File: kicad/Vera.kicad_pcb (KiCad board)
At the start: 3 copper layers, 69.8 x 25.4 mm, 37 parts, among them Q1 AO3400, T1 Wurth 749010012A, T2 Wurth 749010012A, U1 TI AM62A7, U2 Microchip KSZ9477, U3 TI MSPM0G3507, U4 TI ISOW1044BDFMR, U5 Infineon SLB9670, Y1 25MHz

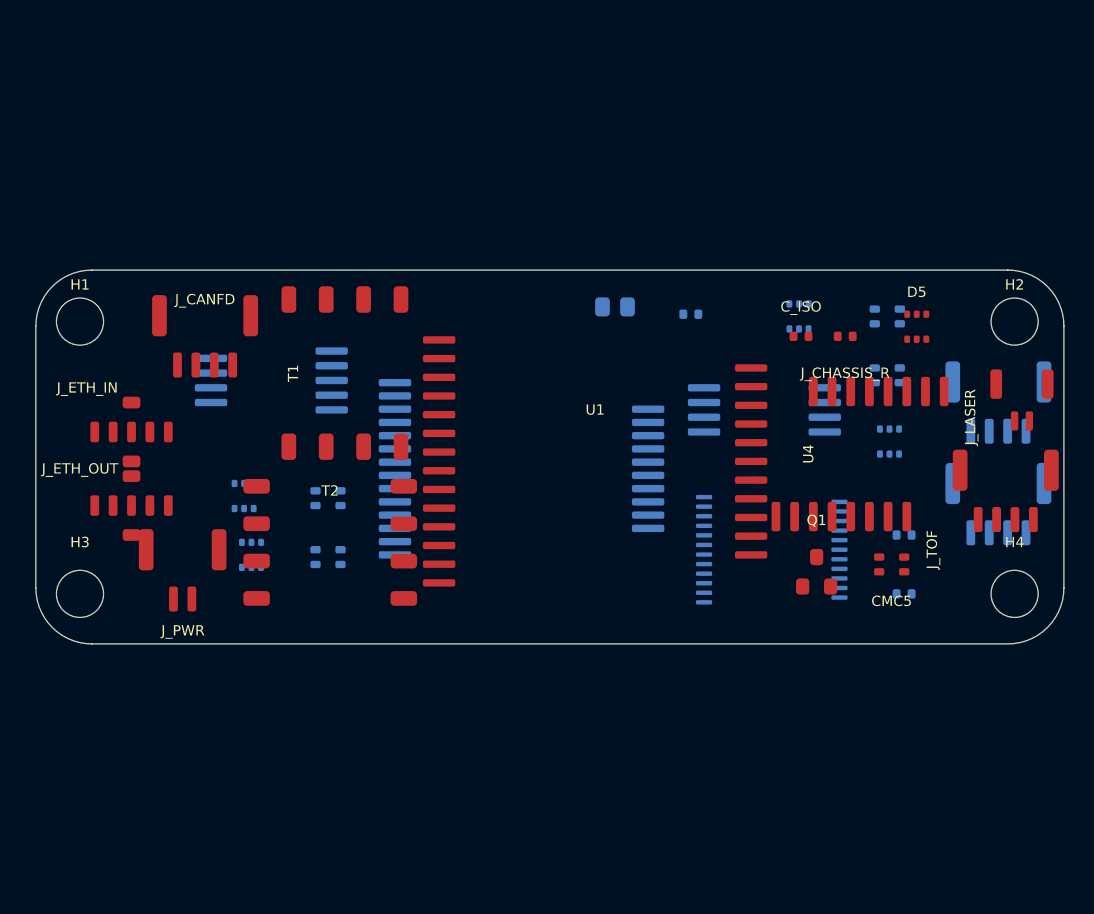
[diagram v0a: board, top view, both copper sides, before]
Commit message: Vera: fix unloadable PCB (restore In2.Cu, rebuild outline) + dot-grid/3D analysis
PCB was committed in a broken state after the 1"-wide (25.4 x 69.85 mm) resize:
- LAYER TABLE was missing In2.Cu(6), leaving an invalid 3-copper-layer stackup ->
  "Failed to load board" (broken across several commits). Restored In2.Cu to the
  4-layer stackup (F.Cu/In1.Cu/In2.Cu/B.Cu), matching Emma. Board loads again.
- Edge.Cuts was malformed/self-intersecting from the resize (invalid_outline x4).
  Rebuilt a clean rounded rectangle 69.85 x 25.4 mm, 3.81 mm corners -> 0 invalid.
- Verified: sch<->pcb net parity is EXACT (88 = 88 nets) -- the nets were never
  scrambled; the board just would not load. Remaining DRC (29 lib_footprint_mismatch,
  silk text) is the pre-existing placeholder-footprint / not-fab-ready state; 106
  unconnected is the never-routed state (routing awaits real footprints).
- Vera.md: corrected the stale mounting-hole coords from the old 46x48 board
  (4,4)/(42,44) -- (42,44) is outside a 25.4 mm-tall board -- to the 69.85x25.4
  pattern (4,4)/(65.85,4)/(4,21.4)/(65.85,21.4).

VERA_LASER_ANALYSIS.md -> Rev B: pattern switched from crosshair to a DOT GRID
(homography for full pose: tilt magnitude+azimuth, no sign ambiguity; cheaper
commodity DOE; better SNR, still Class 2). New cargo TRUE 3D imager (separate
camera+projector by ~75 mm baseline -> ~1.9 mm depth res at 5 ft, pseudo-random
dots); nose stays boresighted grid (baseline useless at 50 ft). Manufacturer notes
(LaserLand / HOLO/OR / Osela / Edmund).

Co-Authored-By: Claude Opus 4.8 <noreply@anthropic.com>
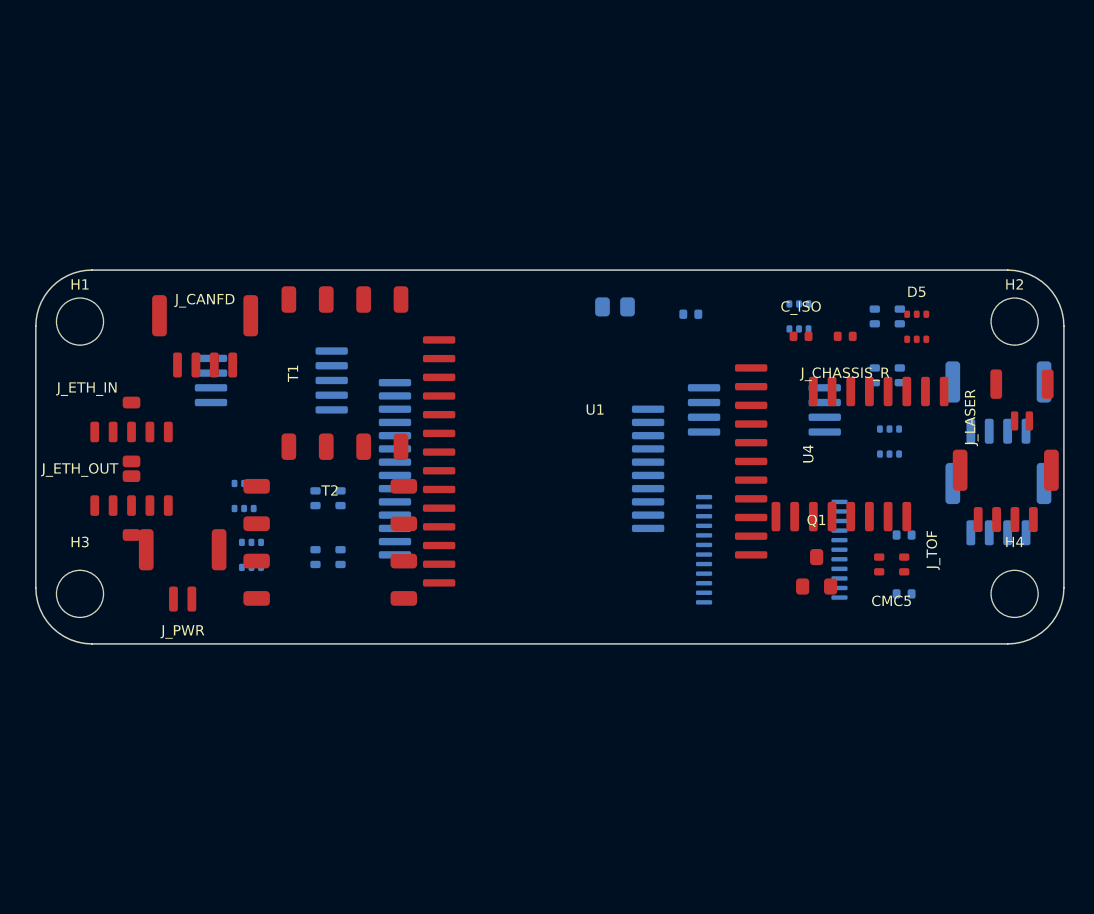
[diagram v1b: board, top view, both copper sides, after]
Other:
- copper layers 3 -> 4
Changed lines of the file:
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@@
 		(0 "F.Cu" signal)
 		(4 "In1.Cu" power)
+		(6 "In2.Cu" power)
 		(2 "B.Cu" power)
 		(9 "F.Adhes" user "F.Adhesive")
@@
 		(embedded_fonts no)
 	)
-	(gr_arc
-		(start 3.81 25.4)
-		(mid 1.115923 24.284077)
-		(end 0 21.59)
-		(stroke
-			(width 0.05)
-			(type solid)
-		)
-		(layer "Edge.Cuts")
-	)
 	(gr_line
 		(start 3.81 0)
-		(end 66.04 0)
+		(end 66.039999 0)
 		(stroke
-			(width 0.05)
-			(type solid)
+			(width 0.1)
+			(type default)
 		)
 		(layer "Edge.Cuts")
 	)
 	(gr_line
-		(start 69.85 3.81)
-		(end 69.85 21.59)
+		(start 66.039999 25.4)
+		(end 3.81 25.4)
 		(stroke
-			(width 0.05)
-			(type solid)
+			(width 0.1)
+			(type default)
 		)
 		(layer "Edge.Cuts")
 	)
-	(gr_line
-		(start 65.989353 25.399663)
-		(end 3.81 25.4)
+	(gr_arc
+		(start 66.039999 0)
+		(mid 68.734076 1.115923)
+		(end 69.85 3.81)
 		(stroke
-			(width 0.05)
-			(type solid)
+			(width 0.1)
+			(type default)
 		)
 		(layer "Edge.Cuts")
 	)
-	(gr_line
-		(start 0 21.59)
-		(end 0 3.81)
+	(gr_arc
+		(start 69.85 21.59)
+		(mid 68.734076 24.284076)
+		(end 66.039999 25.4)
 		(stroke
-			(width 0.05)
-			(type solid)
+			(width 0.1)
+			(type default)
 		)
 		(layer "Edge.Cuts")
@@
 		(end 3.81 0)
 		(stroke
-			(width 0.05)
-			(type solid)
+			(width 0.1)
+			(type default)
 		)
 		(layer "Edge.Cuts")
 	)
-	(gr_arc
-		(start 66.04 0)
-		(mid 68.734077 1.115923)
-		(end 69.85 3.81)
+	(gr_line
+		(start 69.85 3.81)
+		(end 69.85 21.59)
 		(stroke
-			(width 0.05)
-			(type solid)
+			(width 0.1)
+			(type default)
+		)
+		(layer "Edge.Cuts")
+	)
+	(gr_line
+		(start 0 21.59)
+		(end 0 3.81)
+		(stroke
+			(width 0.1)
+			(type default)
 		)
 		(layer "Edge.Cuts")
 	)
 	(gr_arc
-		(start 69.85 21.59)
-		(mid 68.734077 24.284077)
-		(end 66.04 25.4)
+		(start 3.81 25.4)
+		(mid 1.115923 24.284076)
+		(end 0 21.59)
 		(stroke
-			(width 0.05)
-			(type solid)
+			(width 0.1)
+			(type default)
 		)
 		(layer "Edge.Cuts")

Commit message: Vera: place direct-solder sensor lands on the PCB (pcbnew transform)
mod_vera_ds_pcb.py adds J_TOF_DS/J_LASER_DS/J_CAM_DS (from Vera.pretty) to the
hand-maintained Vera.kicad_pcb in place (NOT regenerated -- the board is GUI-owned
and carries the In2.Cu/outline hand-fixes). Each pad is netted to its JST
counterpart's exact net (verified: CSI_CLK_*/CSI_D0_*/CAM_*/+3V3/GND on the camera
land; +5V/GND/UART_TOF_* on ToF; +5V/LASER_CATHODE on laser).

Verified after transform: board loads in kicad-cli; copper stackup intact
(F.Cu/In1.Cu/In2.Cu/B.Cu -- In2.Cu preserved, no recurrence of the drop bug);
invalid_outline = 0.

Lands seeded in a row at the aperture-relative X spacing (ToF..laser 8.2mm,
ToF..camera 16.5mm per bow_sensor_pod.scad). FINAL XY/rotation + which edge faces
the pod is a MANUAL mechanical fit to the sensor mounting plate -- any placement
overlap/clearance DRC on this tightly-packed board is referred to the user per the
project footprint-placement rule.

Co-Authored-By: Claude Opus 4.8 <noreply@anthropic.com>
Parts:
- added J_CAM_DS: DS_Camera_9P, DS_Camera_9P, F.Cu at (21.0, 6.00)
- added J_LASER_DS: DS_Laser_2P, DS_Laser_2P, F.Cu at (12.7, 6.00)
- added J_TOF_DS: DS_ToF_4P, DS_ToF_4P, F.Cu at (4.50, 6.00)

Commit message: Vera: align direct-solder lands to board frame (port-starboard Y spread)
Per the Vera board frame (user): +X fore->aft, +Y starboard->port, +Z
ventral->dorsal; sensors forward, network aft. The three nose apertures differ in
the PORT-STARBOARD (Y) axis, so the lands are respread along Y (not X as first
seeded), co-located with their sensor JST counterparts:
  J_TOF_DS   Y=5.0   (starboard, low Y)
  J_LASER_DS Y=13.2  (centreline, +8.2mm)   <- aperture spacing, bow_sensor_pod.scad
  J_CAM_DS   Y=21.5  (port, +16.5mm)
all at X=62 (just inboard of the sensor JST cluster at X~65-67).
mod_vera_ds_pcb.py now repositions idempotently. Board loads; In2.Cu + outline
intact; nets unchanged.

FLAG -- fore/aft mismatch to resolve: the current board places the SENSOR
connectors at HIGH X (~65-67) and the NETWORK connectors at LOW X (~6-11). Per the
stated convention (sensors forward = low X, network aft = high X) this is
FORE-AFT-FLIPPED. The DS lands are co-located with the sensors as-built (high X);
if the board should match the convention, the whole sensor/network cluster
assignment needs to swap ends -- referred to user.

Co-Authored-By: Claude Opus 4.8 <noreply@anthropic.com>
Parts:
- moved J_TOF_DS 57.5 mm to (62.0, 5.00)
- moved J_LASER_DS 49.8 mm to (62.0, 13.2)
- moved J_CAM_DS 43.8 mm to (62.0, 21.5)
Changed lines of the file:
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@@
 	(footprint "DS_Camera_9P"
 		(layer "F.Cu")
-		(at 21 6)
+		(at 62 21.5)
 		(property "Reference" "J_CAM_DS"
 			(at 0 -2.2 0)
@@
 	(footprint "DS_Laser_2P"
 		(layer "F.Cu")
-		(at 12.7 6)
+		(at 62 13.2)
 		(property "Reference" "J_LASER_DS"
 			(at 0 -2.2 0)
@@
 	(footprint "DS_ToF_4P"
 		(layer "F.Cu")
-		(at 4.5 6)
+		(at 62 5)
 		(property "Reference" "J_TOF_DS"
 			(at 0 -2.2 0)

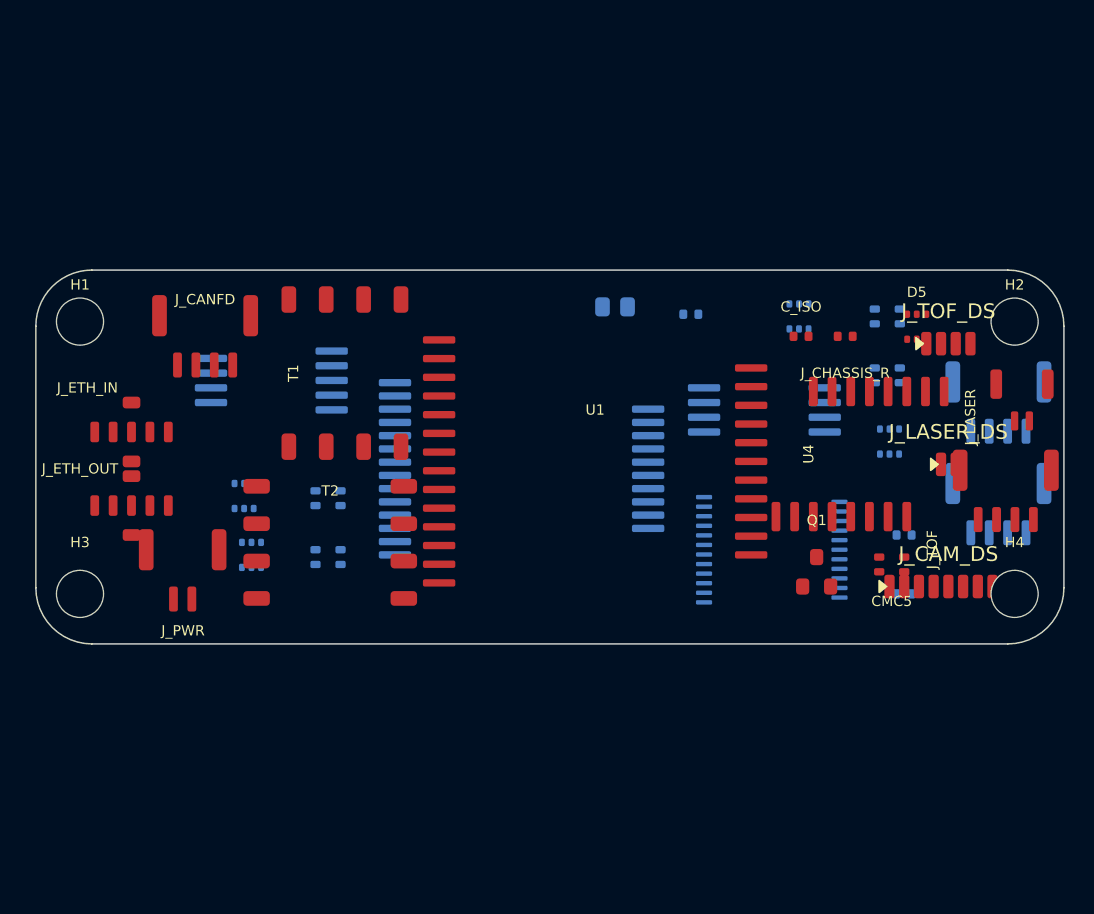
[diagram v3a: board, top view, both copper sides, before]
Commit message: Vera: redraw PCB outline as the nose trapezoid (candidate)
mod_vera_trapezoid.py redraws Edge.Cuts as the trapezoid from
docs/VERA_NOSE_TRAPEZOID.md Rev B: narrow 25.4mm at the fwd/sensor end (high X),
widening to 58mm at the aft end (low X), 69.85mm long, symmetric about the board
centreline (~aircraft CL). Fits the measured ~58mm usable nose interior and holds
the 40x40 SoM at the aft end.

Verified: board loads (pre-commit guard), invalid_outline=0, copper stackup intact
(In2.Cu preserved). Outline extents X -0.1..69.9, Y -16.4..41.8. This is a CANDIDATE
straight trapezoid; a fast-widening/two-segment nose-following edge is the FreeCAD
refinement (doc 4.1/6). Existing placeholder footprints not yet re-placed -> the
edge-clearance DRC delta is expected and resolves when components are laid out for
the trapezoid (gated on the SoM 270-pad DSC + ISOW1044 DFM-20 footprints).

Co-Authored-By: Claude Opus 4.8 <noreply@anthropic.com>
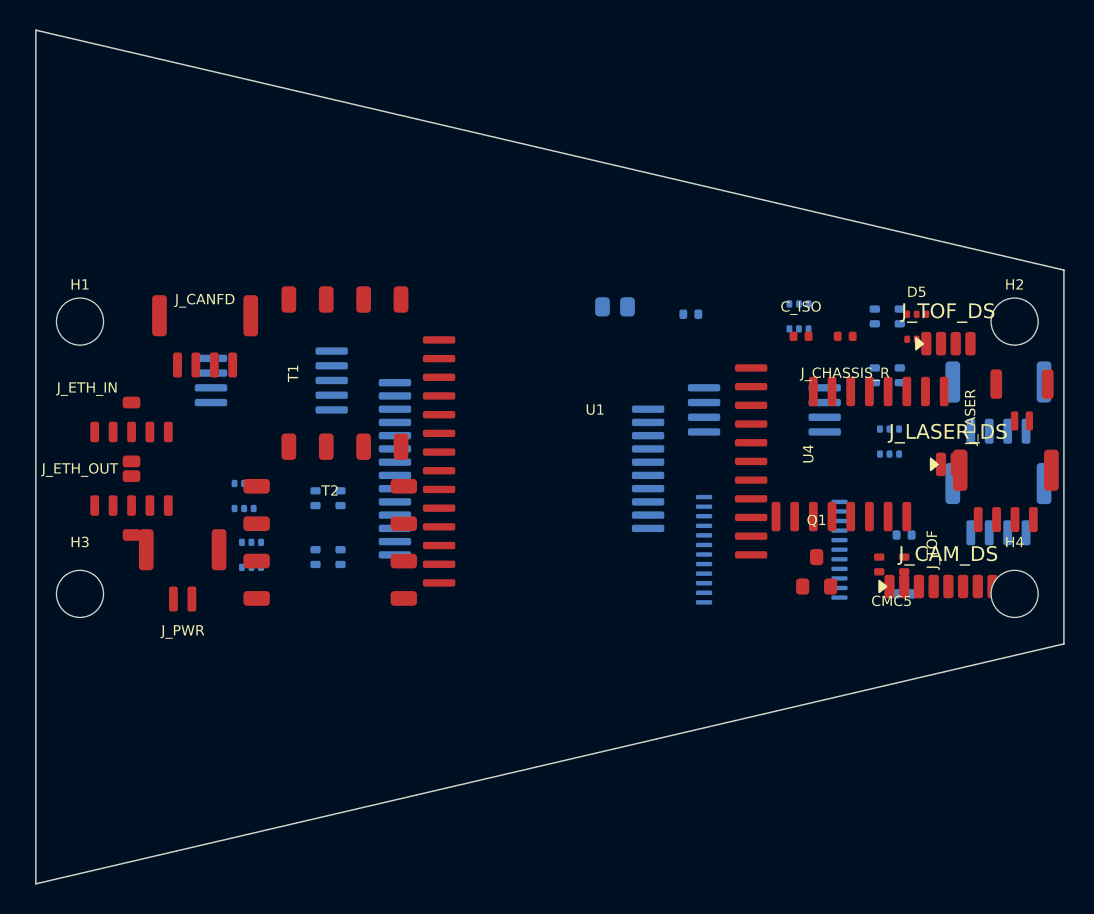
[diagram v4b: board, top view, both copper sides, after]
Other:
- board size 69.8 x 25.4 mm -> 69.8 x 58 mm
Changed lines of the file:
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@@
 	)
 	(gr_line
-		(start 3.81 0)
-		(end 66.039999 0)
+		(start 0 -16.3)
+		(end 69.85 0)
 		(stroke
 			(width 0.1)
@@
 	)
 	(gr_line
-		(start 66.039999 25.4)
-		(end 3.81 25.4)
-		(stroke
-			(width 0.1)
-			(type default)
-		)
-		(layer "Edge.Cuts")
-	)
-	(gr_arc
-		(start 66.039999 0)
-		(mid 68.734076 1.115923)
-		(end 69.85 3.81)
-		(stroke
-			(width 0.1)
-			(type default)
-		)
-		(layer "Edge.Cuts")
-	)
-	(gr_arc
-		(start 69.85 21.59)
-		(mid 68.734076 24.284076)
-		(end 66.039999 25.4)
-		(stroke
-			(width 0.1)
-			(type default)
-		)
-		(layer "Edge.Cuts")
-	)
-	(gr_arc
-		(start 0 3.81)
-		(mid 1.115923 1.115923)
-		(end 3.81 0)
+		(start 0 41.7)
+		(end 0 -16.3)
 		(stroke
 			(width 0.1)
@@
 	)
 	(gr_line
-		(start 69.85 3.81)
-		(end 69.85 21.59)
+		(start 69.85 25.4)
+		(end 0 41.7)
 		(stroke
 			(width 0.1)
@@
 	)
 	(gr_line
-		(start 0 21.59)
-		(end 0 3.81)
+		(start 69.85 0)
+		(end 69.85 25.4)
 		(stroke
 			(width 0.1)
-			(type default)
-		)
-		(layer "Edge.Cuts")
-	)
-	(gr_arc
-		(start 3.81 25.4)
-		(mid 1.115923 24.284076)
-		(end 0 21.59)
-		(stroke
-			(width 0.1)

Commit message: Vera: place PCM-071 SoM at aft/wide end -- initial two-sided fit confirmed
mod_vera_som_place.py adds U_SOM (phyCORE-AM62x PCM-071 placement footprint, 32x43)
at the aft/wide end (board X=24, Y=12.7, rot90 so 43mm runs fore-aft). Verified the
32mm-wide module fits the nose trapezoid: 36.8mm board width at the SoM forward edge
vs 32mm needed; ~57mm at the aft. Board loads (pre-commit guard), invalid_outline=0,
stackup intact.

Initial 2-sided fit: SoM + sensor DS lands/JSTs (fwd) + network conns (aft) all fit
the trapezoid. Old raw-SoC placeholders (U1 AM62A7, U_PMIC) not yet removed -> their
overlap DRC is expected and clears in the full connector-variant re-layout (drop
raw-SoC parts, add the Samtec BTH-060 land pattern + carrier ICs, wire per net map).

Co-Authored-By: Claude Opus 4.8 <noreply@anthropic.com>
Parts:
- added U_SOM: phyCORE-AM62x_PCM071, phyCORE-AM62x_PCM071_placement, F.Cu at (24.0, 12.7)
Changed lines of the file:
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@@
+		(embedded_fonts no)
+	)
+	(footprint "phyCORE-AM62x_PCM071_placement"
+		(layer "F.Cu")
+		(at 24 12.7 90)
+		(descr "PHYTEC phyCORE-AM62x PCM-071 connectorized SoM -- PLACEMENT footprint (outline + 2x M2.5 mounting holes + 2 Samtec BTH-060 connector reference zones) from PHYTEC HW manual L-1038e.A5 Figs 3/6/7. For fit/placement only; the 240 BTH-060 solder pads (A1..D60, 0.5mm pitch 2x60 x2) require the Samtec BTH-060-01-L-D-A-K-TR land pattern -- author before routing. 32x43mm, 5mm connector stacking height.")
+		(property "Reference" "U_SOM"
+			(at 0 -23 90)
+			(layer "F.SilkS")
+			(effects
+				(font
+					(size 1 1)
+					(thickness 0.15)
+				)
+			)
+		)
+		(property "Value" "phyCORE-AM62x_PCM071"
+			(at 0 23 90)
+			(layer "F.Fab")
+			(effects
+				(font
+					(size 1 1)
+					(thickness 0.15)
+				)
+			)
+		)
+		(property "Datasheet" ""
+			(at 0 0 90)
+			(layer "F.Fab")
+			(hide yes)
+			(effects
+				(font
+					(size 1.27 1.27)
+					(thickness 0.15)
+				)
+			)
+		)
+		(property "Description" ""
+			(at 0 0 90)
+			(layer "F.Fab")
+			(hide yes)
+			(effects
+				(font
+					(size 1.27 1.27)
+					(thickness 0.15)
+				)
+			)
+		)
+		(attr exclude_from_pos_files exclude_from_bom allow_missing_courtyard)
+		(fp_rect
+			(start -16 -21.5)
+			(end 16 21.5)
+			(stroke
+				(width 0.12)
+				(type solid)
+			)
+			(fill no)
+			(layer "F.SilkS")
+		)
+		(fp_poly
+			(pts
+				(xy 11 15) (xy 12 15) (xy 11.5 16)
+			)
+			(stroke
+				(width 0.1)
+				(type solid)
+			)
+			(fill yes)
+			(layer "F.SilkS")
+		)
+		(fp_rect
+			(start -16.25 -21.75)
+			(end 16.25 21.75)
+			(stroke
+				(width 0.05)
+				(type solid)
+			)
+			(fill no)
+			(layer "F.CrtYd")
+		)
+		(fp_rect
+			(start -16 -21.5)
+			(end 16 21.5)
+			(stroke
+				(width 0.12)
+				(type solid)
+			)
+			(fill no)
+			(layer "F.Fab")
+		)
+		(fp_rect
+			(start 10.4 -15)
+			(end 12 15)
+			(stroke
+				(width 0.1)
+				(type solid)
+			)
+			(fill no)
+			(layer "F.Fab")
+		)
+		(fp_rect
+			(start -12 -15)
+			(end -10.4 15)
+			(stroke
+				(width 0.1)
+				(type solid)
+			)
+			(fill no)
+			(layer "F.Fab")
+		)
+		(fp_text user "X1 A/B"
+			(at 11.2 -16.5 90)
+			(layer "F.Fab")
+			(effects
+				(font
+					(size 0.8 0.8)
+					(thickness 0.12)
+				)
+			)
+		)
+		(fp_text user "X1 C/D"
+			(at -11.2 -16.5 90)
+			(layer "F.Fab")
+			(effects
+				(font
+					(size 0.8 0.8)
+					(thickness 0.12)
+				)
+			)
+		)
+		(fp_text user "BTH-060 pads TBD: Samtec land"
+			(at 0 0 90)
+			(layer "F.Fab")
+			(effects
+				(font
+					(size 1 1)
+					(thickness 0.15)
+				)
+			)
+		)
+		(pad "MH1" thru_hole circle
+			(at -13.2 -18.7 90)
+			(size 4 4)
+			(drill 2.6)
+			(layers "*.Cu" "*.Mask")
+			(remove_unused_layers no)
+		)
+		(pad "MH2" thru_hole circle
+			(at 13.2 18.7 90)
+			(size 4 4)
+			(drill 2.6)
+			(layers "*.Cu" "*.Mask")
+			(remove_unused_layers no)
+		)
 		(embedded_fonts no)
 	)
